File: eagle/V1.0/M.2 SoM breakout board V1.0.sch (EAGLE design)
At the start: 118 parts, among them J1 3-PIN SMD, J11 WAFER-HY2.0-4PWB, J18 PARTICLE-STUDIOS_M_SERIES_M.2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, J2 DCJ0202, J21 SIP-2, J3 SPARK_CON_30X2_SMD, J5 SCREW-HOLE-3.7, J6 M.2-SOM-BREAKOUT-BOARD-V0.2-0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, J7 SCREW-HOLE-3.7, Q1 L2N7002, Q2 HSS2333, Q3 HSS2333, Q4 HSS2333, Q5 HSS2333, U1 XC8107, X1 BU-SMA-G, X2 BU-SMA-G, X3 BU-SMA-G, X4 S8111-46R, X5 S8111-46R, X6 S8111-46R

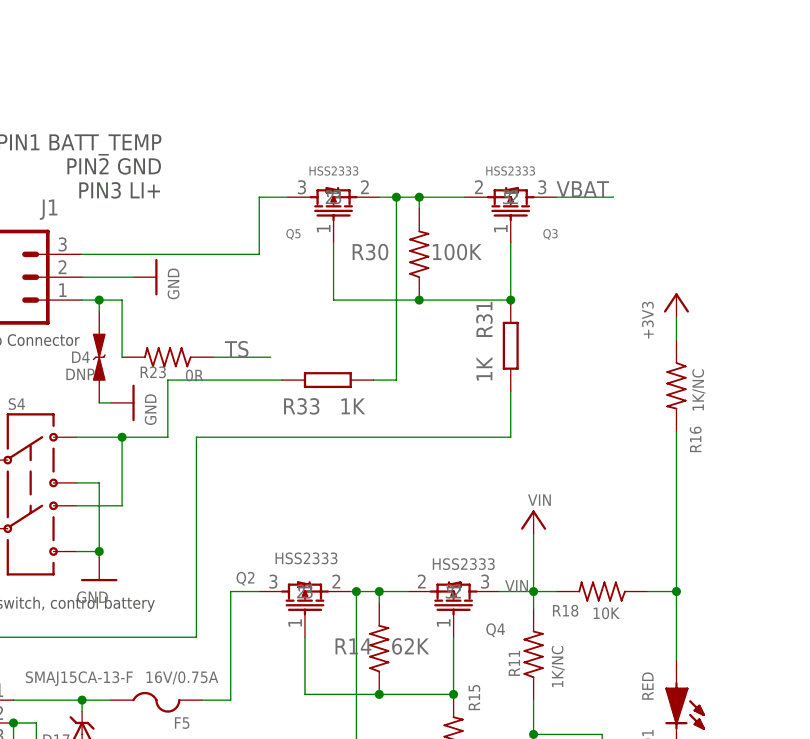
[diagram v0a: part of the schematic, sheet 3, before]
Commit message: Change Q2,Q3,Q4,Q5 value to SI2333DDS
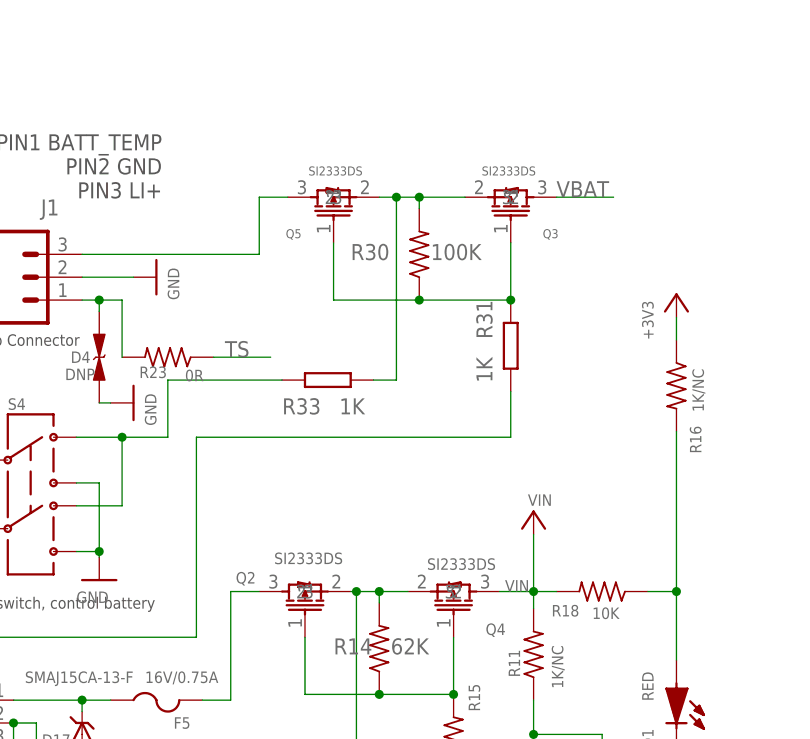
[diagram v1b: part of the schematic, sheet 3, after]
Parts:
- Q2, Q3, Q4, Q5: value HSS2333 -> SI2333DS
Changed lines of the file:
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@@
 <part name="GND35" library="supply1" library_urn="urn:adsk.eagle:library:371" deviceset="GND" device=""/>
 <part name="S1" library="SparkFun-Retired" deviceset="SWITCH-DPDT" device=""/>
-<part name="Q4" library="RedBear" deviceset="PMOS" device="" value="HSS2333"/>
+<part name="Q4" library="RedBear" deviceset="PMOS" device="" value="SI2333DS"/>
 <part name="GND6" library="supply1" library_urn="urn:adsk.eagle:library:371" deviceset="GND" device=""/>
 <part name="R15" library="Particle" deviceset="R-US_" device="" value="36K"/>
@@
 <part name="J21" library="particle SZ" library_urn="urn:adsk.eagle:library:21650216" deviceset="SIP-2" device="" package3d_urn="urn:adsk.eagle:package:21650858/5"/>
 <part name="R30" library="particle-studios" library_urn="urn:adsk.eagle:library:10700396" deviceset="RES_" device="0603" package3d_urn="urn:adsk.eagle:package:10700443/4" technology="100K_" value="100K"/>
-<part name="Q3" library="RedBear" deviceset="PMOS" device="" value="HSS2333"/>
-<part name="Q5" library="RedBear" deviceset="PMOS" device="" value="HSS2333"/>
+<part name="Q3" library="RedBear" deviceset="PMOS" device="" value="SI2333DS"/>
+<part name="Q5" library="RedBear" deviceset="PMOS" device="" value="SI2333DS"/>
 <part name="R31" library="RedBear" deviceset="RES" device="0402S" value="1K"/>
 <part name="LED3" library="particle SZ" deviceset="LED" device="" value="yellow"/>
@@
 <part name="GND21" library="supply1" library_urn="urn:adsk.eagle:library:371" deviceset="GND" device=""/>
 <part name="D4" library="particle SZ" deviceset="ESD" device="" value="DNP"/>
-<part name="Q2" library="RedBear" deviceset="PMOS" device="" value="HSS2333"/>
+<part name="Q2" library="RedBear" deviceset="PMOS" device="" value="SI2333DS"/>
 <part name="R32" library="Particle" deviceset="R-US_" device="" value="1K"/>
 <part name="R14" library="particle-studios" library_urn="urn:adsk.eagle:library:10700396" deviceset="RES_" device="0603" package3d_urn="urn:adsk.eagle:package:10700443/4" technology="100K_" value="62K"/>

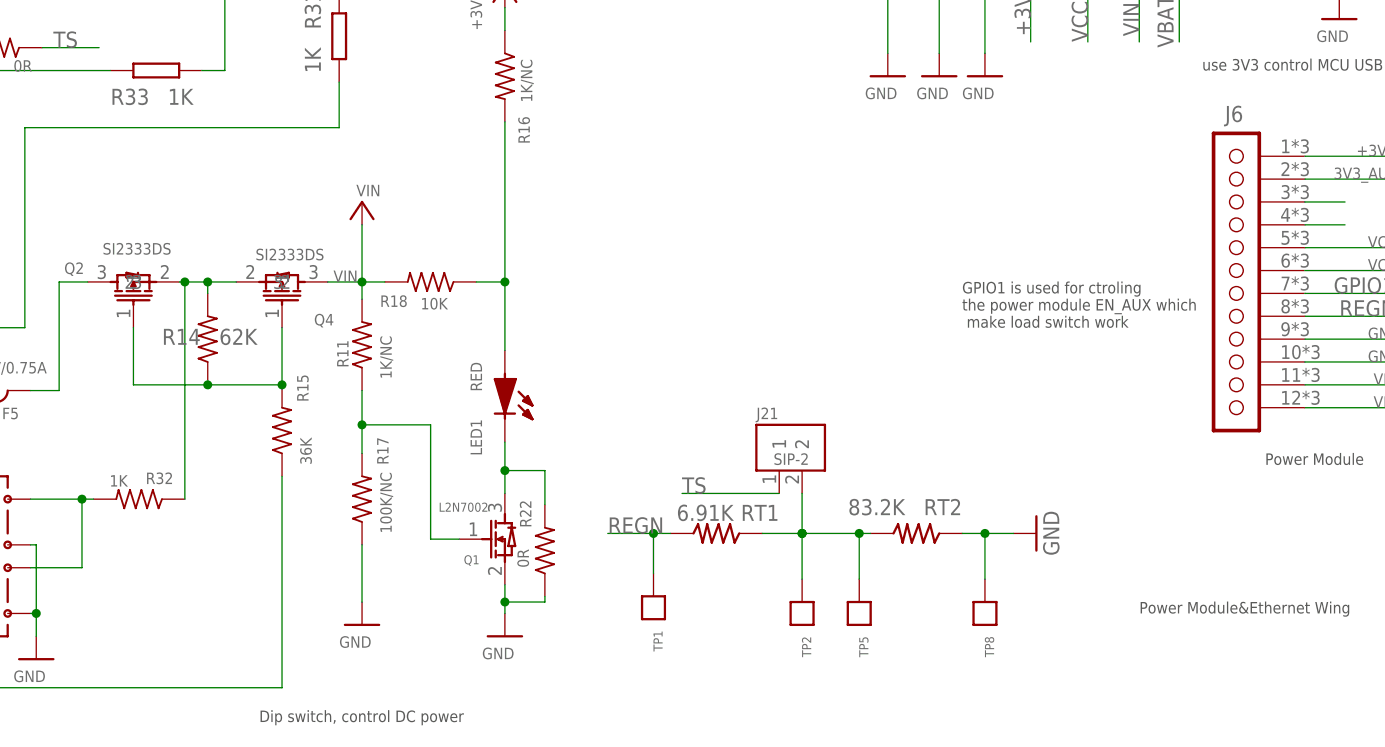
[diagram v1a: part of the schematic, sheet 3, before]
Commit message: Please refer to change list
8.Change J6 PCB package,change drill from 1.016mm to 1.3mm. Smaller pad 0.5mm.
9.Add silkscreen label on the PCB to note that USB is only for comms and not power--"DATA ONLY"
10.Add 3V3_AUX LED.
11.Change PCB version to V1.0.
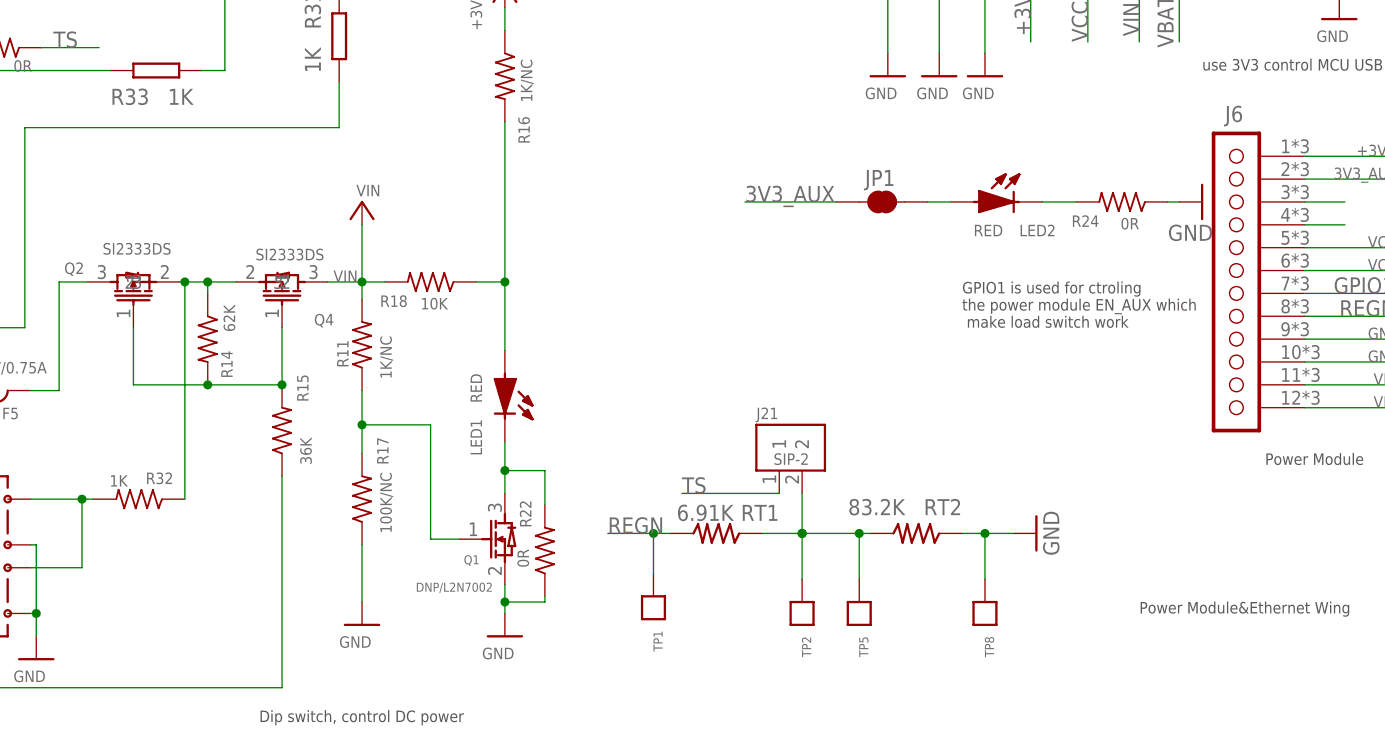
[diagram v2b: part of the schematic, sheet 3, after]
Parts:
- added JP1: JUMPER-SMT_2_NC_TRACE_NO-SILK, SparkFun-Jumpers:JUMPER-SMT_2_NC_TRACE_NO-SILK
- added LED2: RED, particle SZ:LED
- added R24: 0R, Particle:R-US_
- J6: value M.2-SOM-BREAKOUT-BOARD-V0.2-0228_PARTICLE-SZ_PARTICLE-POWER-MODULE -> M.2-SOM-BREAKOUT-BOARD-V0.3_M.2-SOM-BREAKOUT-BOARD-V0.2-0228_PARTICLE-SZ_PARTICLE-POWER-MODULE; device M.2 SoM breakout board v0.3:M.2-SOM-BREAKOUT-BOARD-V0.2-0228_PARTICLE-SZ_PARTICLE-POWER-MODULE -> M.2 SoM breakout board:M.2-SOM-BREAKOUT-BOARD-V0.3_M.2-SOM-BREAKOUT-BOARD-V0.2-0228_PARTICLE-SZ_PARTICLE-POWER-MODULE
- Q1: value L2N7002 -> DNP/L2N7002
- R14: device particle-studios:RES_100K_0603 -> Particle:R-US_
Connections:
- new net N$14: LED2.K, R24.2
- new net N$47: JP1.2, LED2.A
- net 3V3_AUX: now also JP1.1
- net GND: now also R24.1
- net N$10: now also R14.1; no longer R14.2
- net N$17: now also R14.2; no longer R14.1
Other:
- moved on the sheet: R14
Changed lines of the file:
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@@
 <drawing>
 <settings>
-<setting alwaysvectorfont="yes"/>
+<setting alwaysvectorfont="no"/>
 <setting verticaltext="up"/>
 </settings>
@@
 <part name="JP16" library="SparkFun-Jumpers" library_urn="urn:adsk.eagle:library:528" deviceset="JUMPER-SMT_2_NC_TRACE" device="_NO-SILK" package3d_urn="urn:adsk.eagle:package:39286/2"/>
 <part name="D16" library="particle SZ" deviceset="DIODE" device="SOD323" value="PZ3D4V2H"/>
-<part name="Q1" library="particle SZ" deviceset="NMOS" device="SOT323" value="L2N7002"/>
+<part name="Q1" library="particle SZ" deviceset="NMOS" device="SOT323" value="DNP/L2N7002"/>
 <part name="R16" library="Particle" deviceset="R-US_" device="" value="1K/NC"/>
 <part name="+3V2" library="supply1" library_urn="urn:adsk.eagle:library:371" deviceset="+3V3" device=""/>
-<part name="J6" library="M.2 SoM breakout board v0.3" deviceset="M.2-SOM-BREAKOUT-BOARD-V0.2-0228_PARTICLE-SZ_PARTICLE-POWER-MODULE" device=""/>
+<part name="J6" library="M.2 SoM breakout board" deviceset="M.2-SOM-BREAKOUT-BOARD-V0.3_M.2-SOM-BREAKOUT-BOARD-V0.2-0228_PARTICLE-SZ_PARTICLE-POWER-MODULE" device=""/>
 <part name="X4" library="particle-studios" library_urn="urn:adsk.eagle:library:10700396" deviceset="S8111-46R" device=""/>
 <part name="X5" library="particle-studios" library_urn="urn:adsk.eagle:library:10700396" deviceset="S8111-46R" device=""/>
@@
 <part name="Q2" library="RedBear" deviceset="PMOS" device="" value="SI2333DS"/>
 <part name="R32" library="Particle" deviceset="R-US_" device="" value="1K"/>
-<part name="R14" library="particle-studios" library_urn="urn:adsk.eagle:library:10700396" deviceset="RES_" device="0603" package3d_urn="urn:adsk.eagle:package:10700443/4" technology="100K_" value="62K"/>
 <part name="+3V3" library="supply1" library_urn="urn:adsk.eagle:library:371" deviceset="+3V3" device="" value="VIN"/>
 <part name="S2" library="Particle" deviceset="TAC_SWITCH" device=""/>
 <part name="S3" library="Particle" deviceset="TAC_SWITCH" device=""/>
+<part name="LED2" library="particle SZ" deviceset="LED" device="" value="RED"/>
+<part name="R24" library="Particle" deviceset="R-US_" device="" value="0R"/>
+<part name="JP1" library="SparkFun-Jumpers" library_urn="urn:adsk.eagle:library:528" deviceset="JUMPER-SMT_2_NC_TRACE" device="_NO-SILK" package3d_urn="urn:adsk.eagle:package:39286/2"/>
+<part name="GND4" library="supply1" library_urn="urn:adsk.eagle:library:371" deviceset="GND" device=""/>
+<part name="R14" library="Particle" deviceset="R-US_" device="" value="62K"/>
 </parts>
 <sheets>
@@
 <instance part="LED1" gate="G$1" x="92.71" y="41.275" smashed="yes" rot="R270">
 <attribute name="NAME" x="88.9" y="38.735" size="1.27" layer="95" rot="R270"/>
-<attribute name="VALUE" x="88.9" y="45.085" size="1.27" layer="96" rot="R270"/>
+<attribute name="VALUE" x="88.9" y="43.815" size="1.27" layer="96" rot="R270"/>
 </instance>
 <instance part="GND16" gate="1" x="76.835" y="15.875" smashed="yes">
@@
 </instance>
 <instance part="Q1" gate="G$1" x="92.71" y="25.4" smashed="yes">
-<attribute name="VALUE" x="85.344" y="28.448" size="1" layer="96"/>
+<attribute name="VALUE" x="82.804" y="19.558" size="1" layer="96"/>
 <attribute name="NAME" x="88.138" y="22.606" size="1" layer="95"/>
 </instance>
@@
 <attribute name="VALUE" x="50.8" y="32.512" size="1.27" layer="96" rot="R180"/>
 </instance>
-<instance part="R14" gate="R1" x="59.69" y="47.625" smashed="yes" rot="R90">
-<attribute name="NAME" x="54.61" y="46.99" size="1.778" layer="95"/>
-<attribute name="VALUE" x="60.96" y="46.99" size="1.778" layer="96"/>
-</instance>
 <instance part="+3V3" gate="G$1" x="76.835" y="62.865" smashed="yes">
 <attribute name="VALUE" x="76.2" y="63.5" size="1.27" layer="96"/>
 </instance>
+<instance part="LED2" gate="G$1" x="147.32" y="62.865" smashed="yes">
+<attribute name="NAME" x="149.86" y="59.055" size="1.27" layer="95"/>
+<attribute name="VALUE" x="144.78" y="59.055" size="1.27" layer="96"/>
+</instance>
+<instance part="R24" gate="R1" x="161.29" y="62.865" smashed="yes" rot="R180">
+<attribute name="NAME" x="158.75" y="61.3664" size="1.27" layer="95" rot="R180"/>
+<attribute name="VALUE" x="163.195" y="61.087" size="1.27" layer="96" rot="R180"/>
+</instance>
+<instance part="JP1" gate="G$1" x="134.62" y="62.865" smashed="yes">
+<attribute name="NAME" x="132.715" y="64.643" size="1.778" layer="95" font="vector"/>
+</instance>
+<instance part="GND4" gate="1" x="170.18" y="62.865" smashed="yes" rot="MR270">
+<attribute name="VALUE" x="166.37" y="60.325" size="1.778" layer="96" font="vector" rot="MR180"/>
+</instance>
+<instance part="R14" gate="R1" x="59.69" y="47.625" smashed="yes" rot="R270">
+<attribute name="NAME" x="61.1886" y="46.355" size="1.27" layer="95" rot="R270"/>
+<attribute name="VALUE" x="61.468" y="51.435" size="1.27" layer="96" rot="R270"/>
+</instance>
 </instances>
 <busses>
@@
 <junction x="40.64" y="17.145"/>
 </segment>
+<segment>
+<pinref part="GND4" gate="1" pin="GND"/>
+<pinref part="R24" gate="R1" pin="1"/>
+<wire x1="167.64" y1="62.865" x2="166.37" y2="62.865" width="0.1524" layer="91"/>
+</segment>
 </net>
 <net name="+3V3" class="0">
@@
 <wire x1="51.435" y1="48.895" x2="51.435" y2="42.545" width="0.1524" layer="91"/>
 <wire x1="51.435" y1="42.545" x2="59.69" y2="42.545" width="0.1524" layer="91"/>
-<pinref part="R14" gate="R1" pin="1"/>
+<pinref part="R14" gate="R1" pin="2"/>
 <wire x1="59.69" y1="42.545" x2="67.945" y2="42.545" width="0.1524" layer="91"/>
 <junction x="59.69" y="42.545"/>
@@
 <pinref part="J6" gate="G$1" pin="3V3@2"/>
 </segment>
+<segment>
+<pinref part="JP1" gate="G$1" pin="1"/>
+<wire x1="129.54" y1="62.865" x2="119.38" y2="62.865" width="0.1524" layer="91"/>
+<label x="119.38" y="62.865" size="1.778" layer="95"/>
+</segment>
 </net>
 <net name="PWM2" class="0">
@@
 <junction x="57.15" y="53.975"/>
 <pinref part="R32" gate="R1" pin="1"/>
-<pinref part="R14" gate="R1" pin="2"/>
+<pinref part="R14" gate="R1" pin="1"/>
+</segment>
+</net>
+<net name="N$14" class="0">
+<segment>
+<pinref part="R24" gate="R1" pin="2"/>
+<pinref part="LED2" gate="G$1" pin="K"/>
+<wire x1="156.21" y1="62.865" x2="152.4" y2="62.865" width="0.1524" layer="91"/>
+</segment>
+</net>
+<net name="N$47" class="0">
+<segment>
+<pinref part="LED2" gate="G$1" pin="A"/>
+<pinref part="JP1" gate="G$1" pin="2"/>
+<wire x1="142.24" y1="62.865" x2="139.7" y2="62.865" width="0.1524" layer="91"/>
 </segment>
 </net>

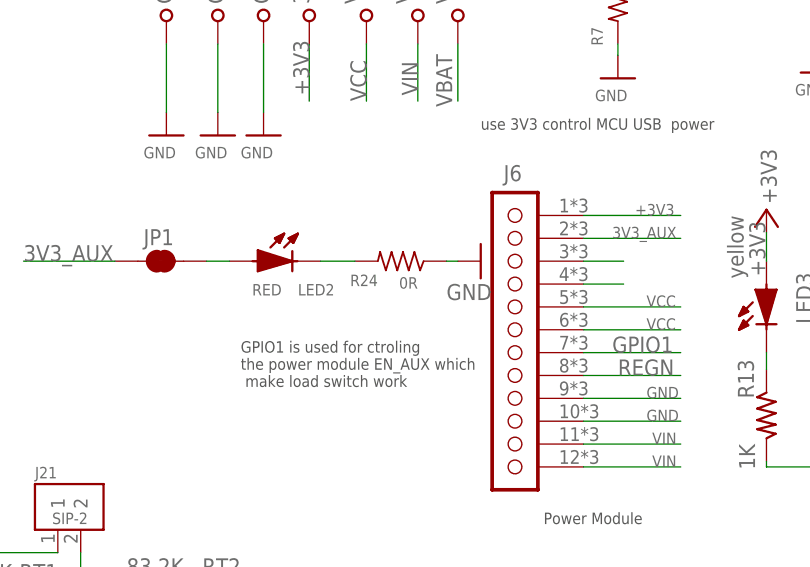
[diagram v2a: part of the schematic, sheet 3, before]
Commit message: change R24 value to 1K.
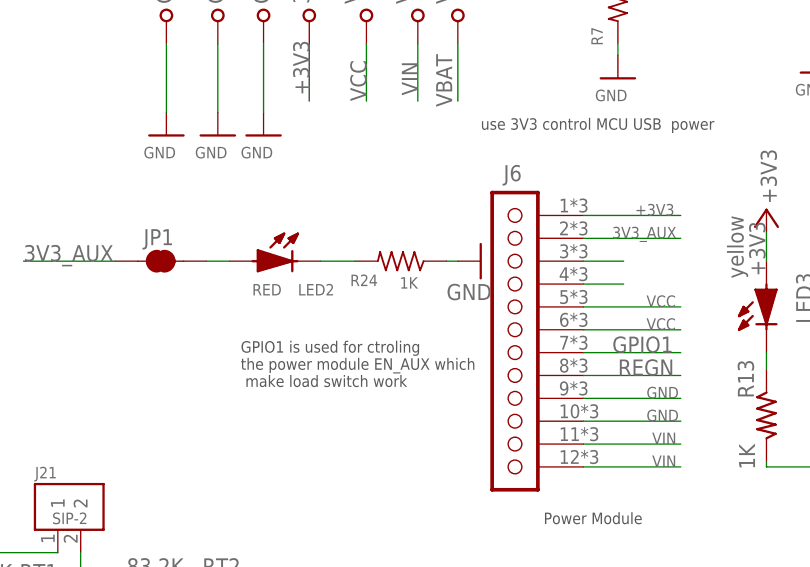
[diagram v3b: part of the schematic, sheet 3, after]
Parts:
- R24: value 0R -> 1K
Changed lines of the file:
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@@
 <part name="S3" library="Particle" deviceset="TAC_SWITCH" device=""/>
 <part name="LED2" library="particle SZ" deviceset="LED" device="" value="RED"/>
-<part name="R24" library="Particle" deviceset="R-US_" device="" value="0R"/>
+<part name="R24" library="Particle" deviceset="R-US_" device="" value="1K"/>
 <part name="JP1" library="SparkFun-Jumpers" library_urn="urn:adsk.eagle:library:528" deviceset="JUMPER-SMT_2_NC_TRACE" device="_NO-SILK" package3d_urn="urn:adsk.eagle:package:39286/2"/>
 <part name="GND4" library="supply1" library_urn="urn:adsk.eagle:library:371" deviceset="GND" device=""/>
